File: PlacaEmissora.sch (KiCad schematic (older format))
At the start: 6 parts, among them J1 JACK_TRS, J2 Screw_Terminal_Laser, J3 Screw_Terminal_Fonte, U1 LM386

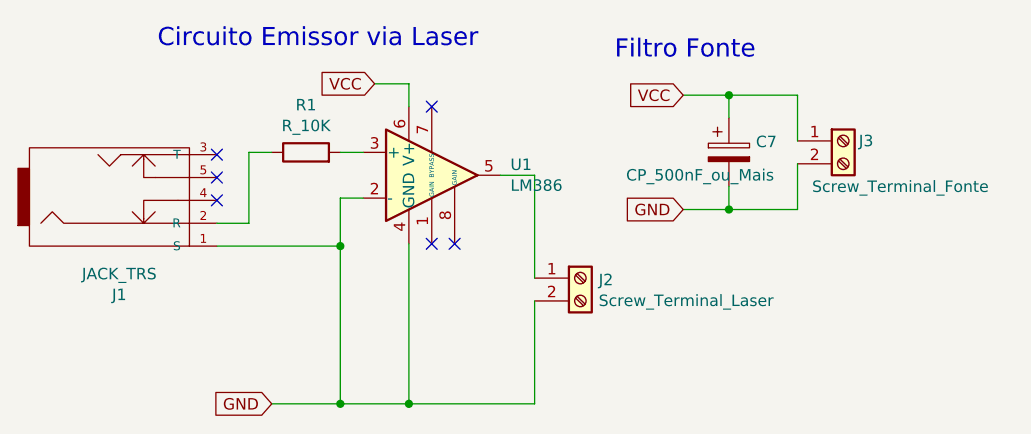
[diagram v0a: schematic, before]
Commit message: Adicionado Botao na placa emissao
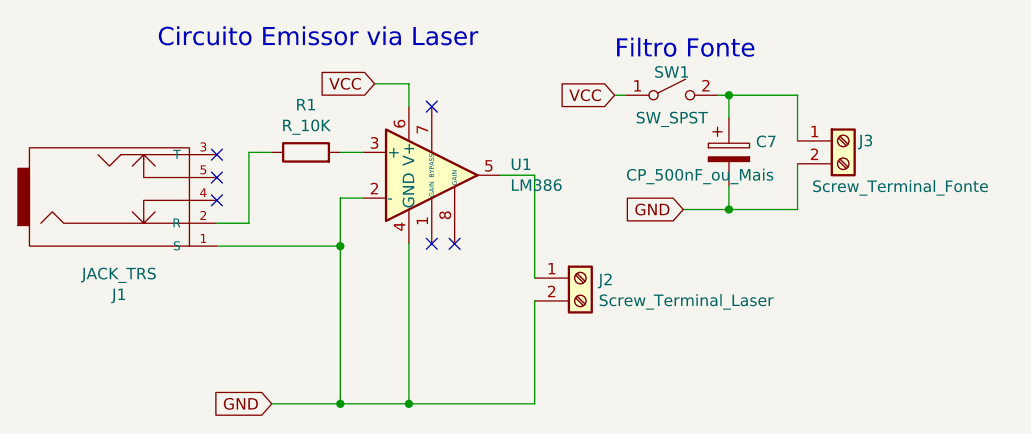
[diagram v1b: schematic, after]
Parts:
- added SW1: SW_SPST, Connector:BotaoOnOff, symbol Switch:SW_SPST
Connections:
- net VCC: now also SW1.1 (A); no longer C7.1, J3.1 (Pin_1)
- new net: C7.1, J3.1 (Pin_1), SW1.2 (B)
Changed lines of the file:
@@
 EESchema Schematic File Version 4
+LIBS:PlacaEmissora-cache
 EELAYER 29 0
 EELAYER END
@@
 Wire Wire Line
 	4800 2950 4700 2950
-Text GLabel 6200 2500 0    50   Input ~ 0
+Text GLabel 5900 2500 0    50   Input ~ 0
 VCC
 Text GLabel 6200 3000 0    50   Input ~ 0
@@
 	6200 3000 6400 3000
 Wire Wire Line
-	6200 2500 6400 2500
-Wire Wire Line
 	6400 2500 6700 2500
 Wire Wire Line
 	6700 2500 6700 2700
-Connection ~ 6400 2500
 Wire Wire Line
 	6700 2800 6700 3000
@@
 	6700 3000 6400 3000
 Connection ~ 6400 3000
+$Comp
+L Switch:SW_SPST SW1
+U 1 1 5DDD0F13
+P 6150 2500
+F 0 "SW1" H 6150 2600 50  0000 C CNN
+F 1 "SW_SPST" H 6150 2400 50  0000 C CNN
+F 2 "Connector:BotaoOnOff" H 6150 2500 50  0001 C CNN
+F 3 "~" H 6150 2500 50  0001 C CNN
+	1    6150 2500
+	1    0    0    -1
+$EndComp
+Wire Wire Line
+	6350 2500 6400 2500
+Connection ~ 6400 2500
+Wire Wire Line
+	5900 2500 5950 2500
 $EndSCHEMATC

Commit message: Feito as pcbs dos circuitos emissor e receptor
Feito os fotolitos da versão V1
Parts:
- SW1: footprint Connector:BotaoOnOff -> Connector:BotaoOnOffMenor
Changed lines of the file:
@@
 F 0 "SW1" H 6150 2600 50  0000 C CNN
 F 1 "SW_SPST" H 6150 2400 50  0000 C CNN
-F 2 "Connector:BotaoOnOff" H 6150 2500 50  0001 C CNN
+F 2 "Connector:BotaoOnOffMenor" H 6150 2500 50  0001 C CNN
 F 3 "~" H 6150 2500 50  0001 C CNN
 	1    6150 2500
